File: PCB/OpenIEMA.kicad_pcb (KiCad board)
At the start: 2 copper layers, 40 x 70 mm, 63 parts, among them J1 Battery, J2 XLR3, J3 USB_C_Receptacle_PowerOnly_6P, J4 AudioJack3, J5 AudioJack3, SW2 SW_SPDT, U1 MCP73831-2-MC, U2 TPS61023DRLR, U3 OPA1678, U4 TPA6132A2RTE

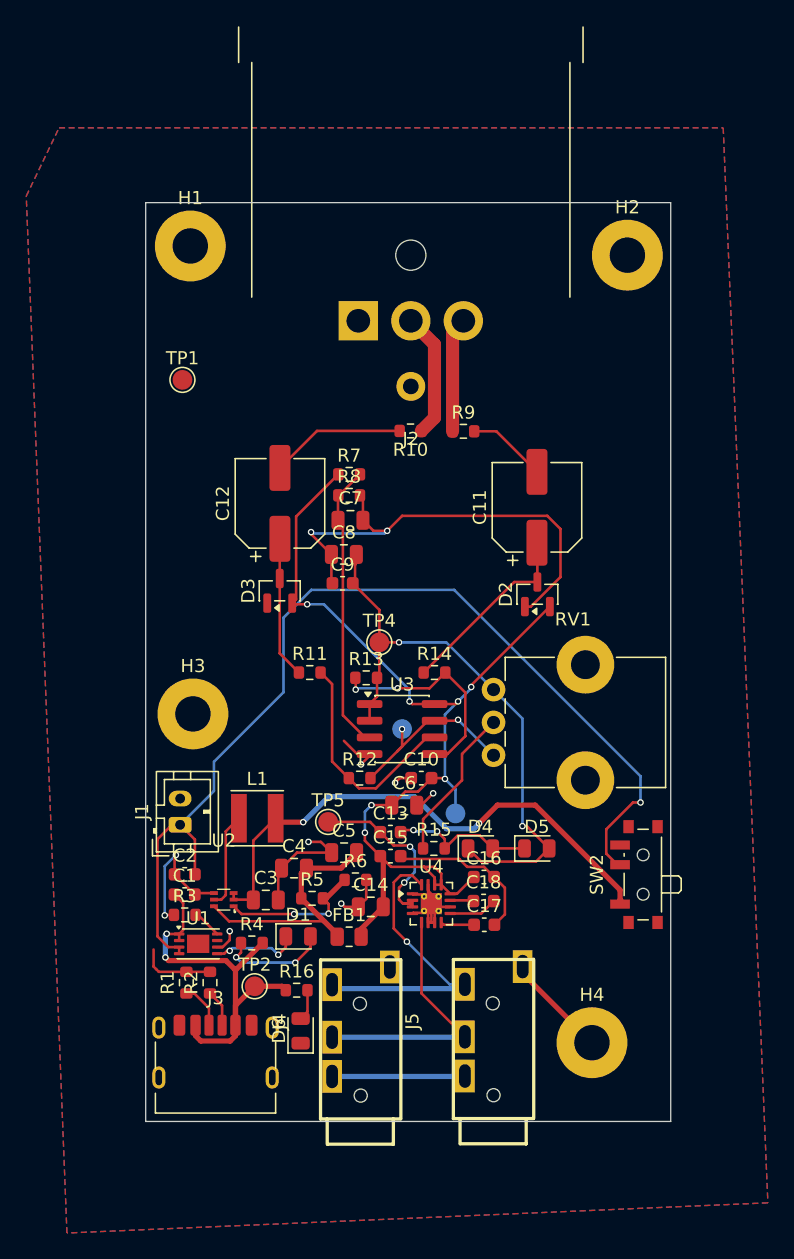
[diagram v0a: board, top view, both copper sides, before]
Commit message: New PCB layout and routing + schematic cleanup
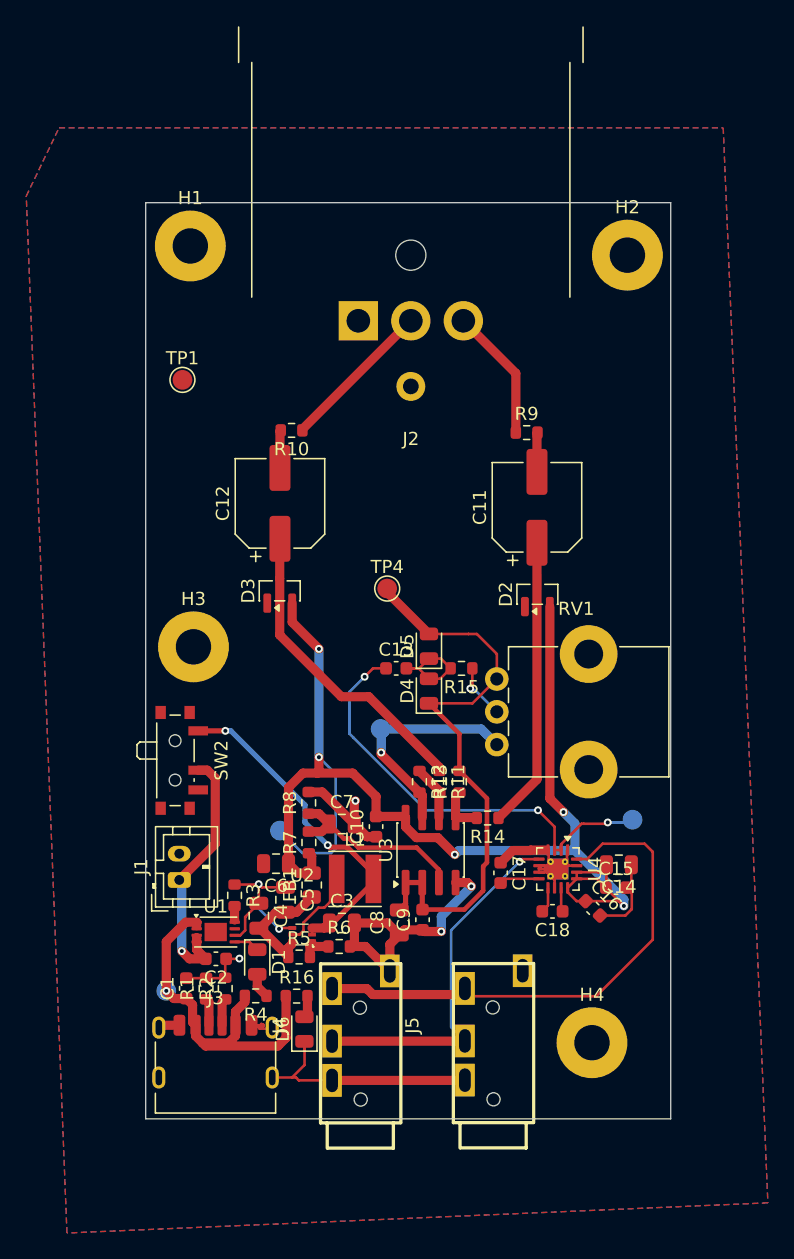
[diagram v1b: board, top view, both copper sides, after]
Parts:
- L1: footprint Inductor_SMD:L_Taiyo-Yuden_NR-40xx -> Fixed_3D:L_Taiyo-Yuden_NR-40xx
- TP2, TP5: moved to B.Cu
- U1: footprint Package_DFN_QFN:DFN-8-1EP_3x2mm_P0.5mm_EP1.7x1.4mm -> Fixed_3D:DFN-8-1EP_3x2mm_P0.5mm_EP1.7x1.4mm
- moved SW2 36.1 mm to (152.1, 93.0), turned to -90 degrees
- moved C8 28.4 mm to (168.8, 105.3), turned to 90 degrees
- moved R7 28.2 mm to (161.9, 99.2), turned to 90 degrees
- moved C9 26.3 mm to (170.6, 105.1), turned to 90 degrees
- moved R8 23.6 mm to (161.9, 96.2), turned to 90 degrees
- moved TP5 23.2 mm to (186.6, 97.5), turned to 180 degrees
- moved C7 23.1 mm to (164.4, 97.8)
- moved C14 19.2 mm to (185.6, 100.9), turned to 180 degrees
- moved D5 17.5 mm to (171.1, 84.3), turned to 90 degrees
- moved C15 17.3 mm to (185.3, 102.7)
- moved R15 13.9 mm to (173.6, 86.0), turned to 180 degrees
- moved TP3 13.4 mm to (159.7, 98.3)
- moved R11 12.9 mm to (171.9, 94.6), turned to -90 degrees
- moved D4 12.6 mm to (171.1, 87.7), turned to 90 degrees
- moved C13 12.5 mm to (168.6, 86.0)
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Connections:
- C17 pad 1: Net-(U4-HPVSS) -> GND
- C17 pad 2: GND -> Net-(U4-HPVSS)
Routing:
- net Net-(J1-Pin_1): track 78.2 -> 19.9 mm
- net GND: track 118.2 -> 91.4 mm, vias 10 -> 6
- net +5VA: track 76.6 -> 102.5 mm, vias 7 -> 5
- net AMP_IN: track 14.3 -> 34.2 mm, vias 2 -> 3
- net VBAT_SW: track 41.8 -> 25.9 mm
- net HP_L: track 24.6 -> 40.1 mm, vias 1 -> 0
- net Net-(U3B--): track 17.4 -> 4.20 mm
- net IN_COLD: track 10.8 -> 24.0 mm
- net Net-(U3B-+): track 16.7 -> 3.66 mm, vias 2 -> 0
- net +5V: track 19.7 -> 9.32 mm
- net Net-(U2-FB): track 11.1 -> 2.40 mm, vias 2 -> 0
- net HP_R: track 20.3 -> 27.9 mm, vias 0 -> 1
- net IN_HOT: track 14.5 -> 22.2 mm
- net VBIAS_RAW: track 22.0 -> 14.5 mm
- net Net-(R15-Pad1): track 11.8 -> 4.36 mm, vias 0 -> 1
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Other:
- board size 40 x 70 mm -> 40 x 69.8 mm

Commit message: New steps + silkscreen
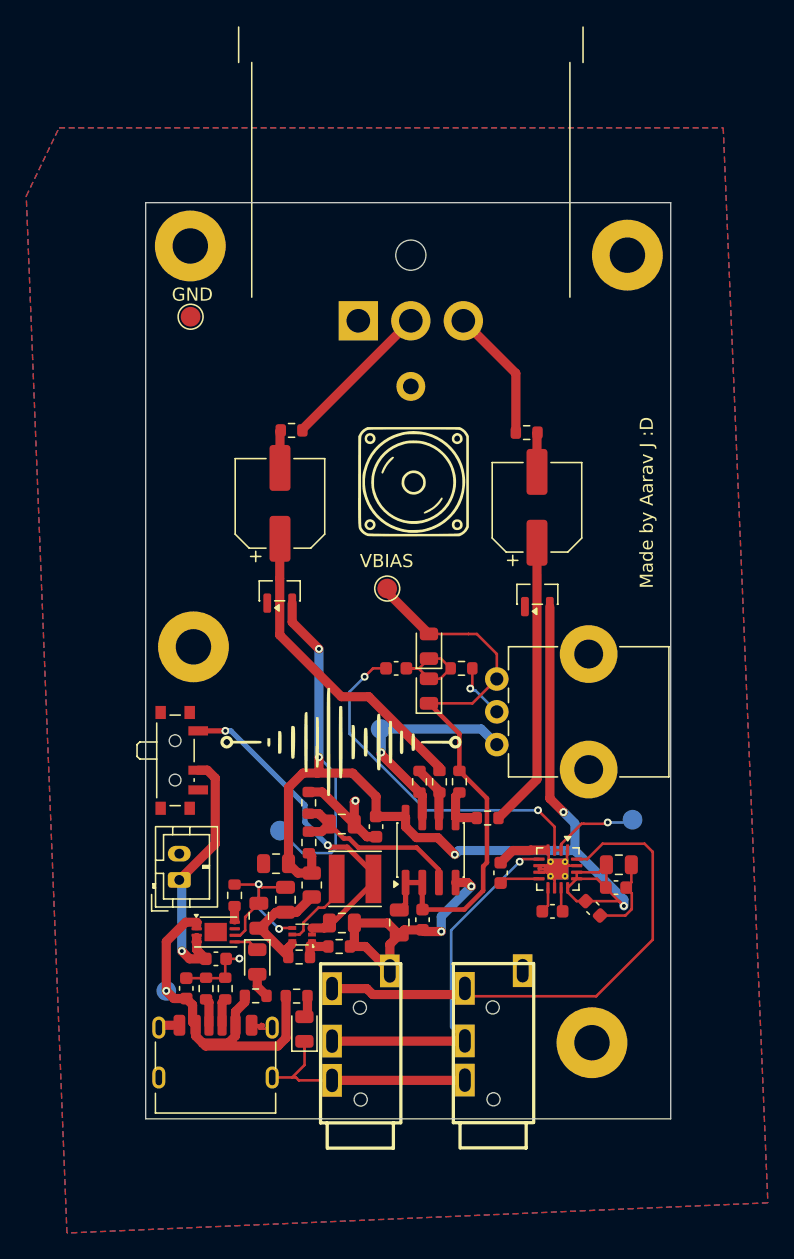
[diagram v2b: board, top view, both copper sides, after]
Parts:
- added G***: LOGO, LOGO, F.Cu at (164.4, 91.4)
- added G***: LOGO, LOGO, F.Cu at (169.8, 71.6)
- added G***: LOGO, LOGO, B.Cu at (170.1, 84.6)
- moved TP1 4.85 mm to (152.9, 59.2)
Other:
- board text added: "+5VA"
- board text added: "AUD"
- board text added: "Amp In"
- board text added: "GND"
- board text added: "Made by Aarav J :D"
- board text added: "VBIAS"
- board text added: "VBUS"
